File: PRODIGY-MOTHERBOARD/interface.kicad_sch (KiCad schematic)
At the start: 28 parts, among them J1 KEYPAD_MATRIX, J2 Conn_01x10, Q1 Q_Photo_NPN, SW1 SW_SPST, SW2 SW_SPST, SW3 SW_SPST, SW4 SW_SPST, SW5 SW_SPST, U1 CR2013-MI2120

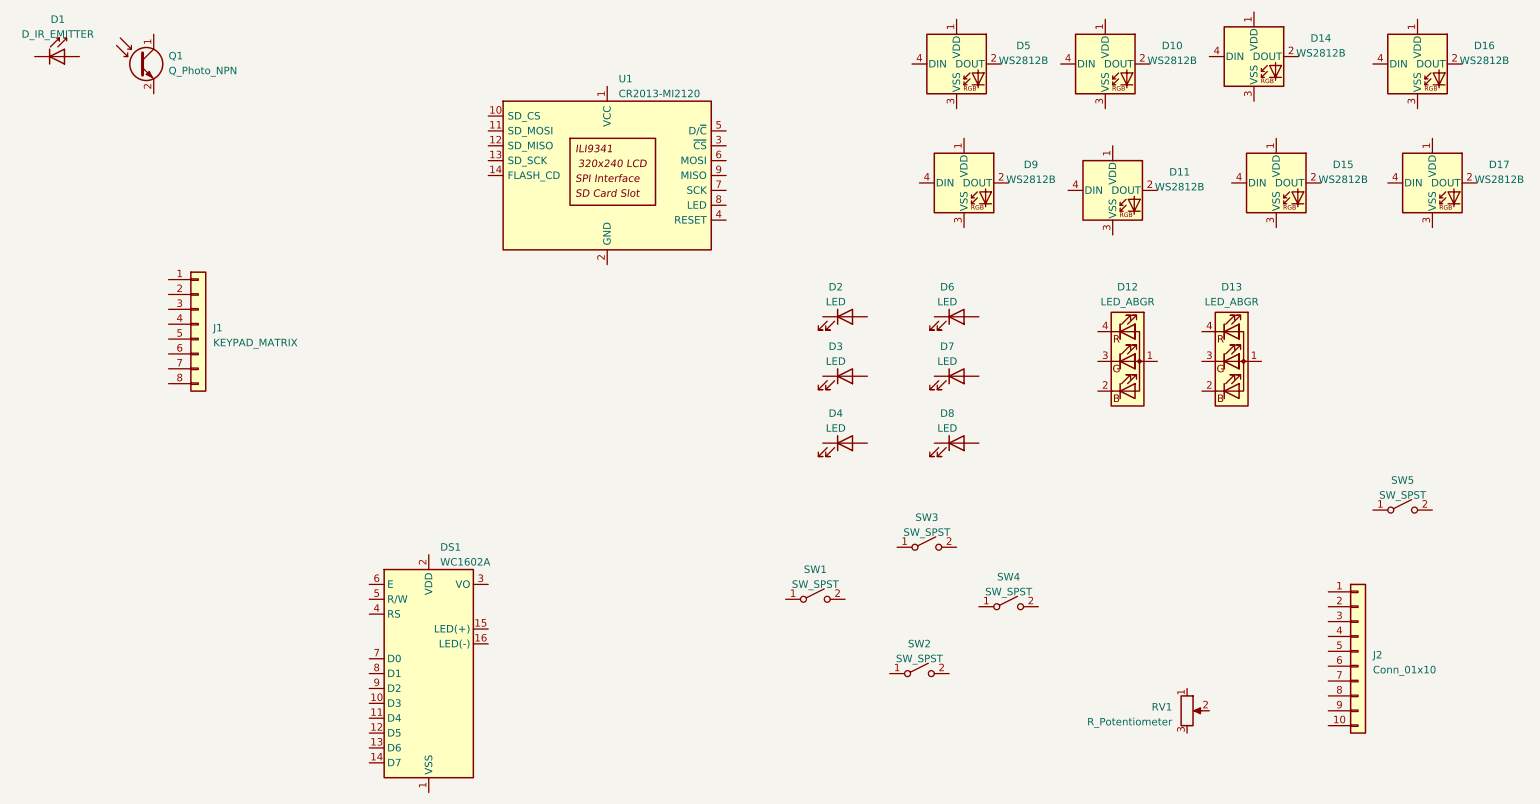
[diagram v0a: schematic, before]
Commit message: project restructure done. Hierarchical sheet done. Outputs/breakouts sheet done
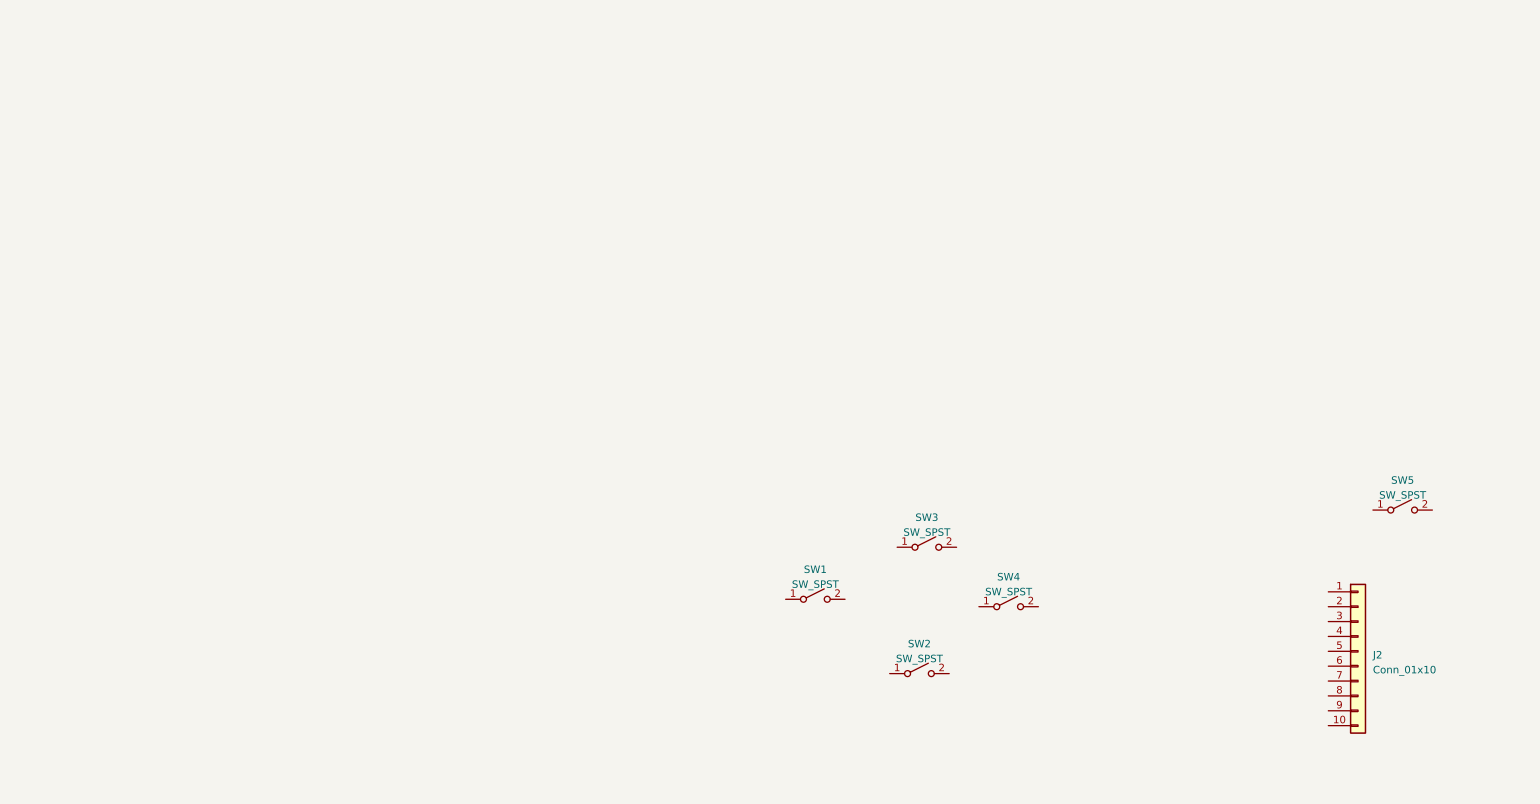
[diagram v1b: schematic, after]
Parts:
- removed D1: D_IR_EMITTER, LED_THT:LED_D5.0mm_Horizontal_O1.27mm_Z3.0mm_Clear, symbol LED:IRL81A
- removed D10, D11, D14, D15, D16, D17, D5, D9: WS2812B, LED_SMD:LED_WS2812B_PLCC4_5.0x5.0mm_P3.2mm, symbol LED:WS2812B
- removed D12, D13: LED_ABGR, LED_THT:LED_D5.0mm-4_RGB, symbol Device:LED_ABGR
- removed D2, D3, D4, D6, D7, D8: LED, LED_THT:LED_D5.0mm, symbol Device:LED
- removed DS1: WC1602A, Display:WC1602A, symbol Display_Character:WC1602A
- removed J1: KEYPAD_MATRIX, Connector_PinHeader_2.54mm:PinHeader_1x08_P2.54mm_Vertical_SMD_Pin1Left, symbol Connector_Generic:Conn_01x08
- removed Q1: Q_Photo_NPN, LED_THT:LED_D5.0mm_Horizontal_O1.27mm_Z3.0mm_IRBlack, symbol Device:Q_Photo_NPN
- removed RV1: R_Potentiometer, Potentiometer_THT:Potentiometer_Piher_PT-15-V15_Vertical, symbol Device:R_Potentiometer
- removed U1: CR2013-MI2120, Display:CR2013-MI2120, symbol Driver_Display:CR2013-MI2120
